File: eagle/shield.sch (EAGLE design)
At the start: 36 parts, among them Q1 REG1117, U1 TXB0104PWR, U2 TXB0104PWR

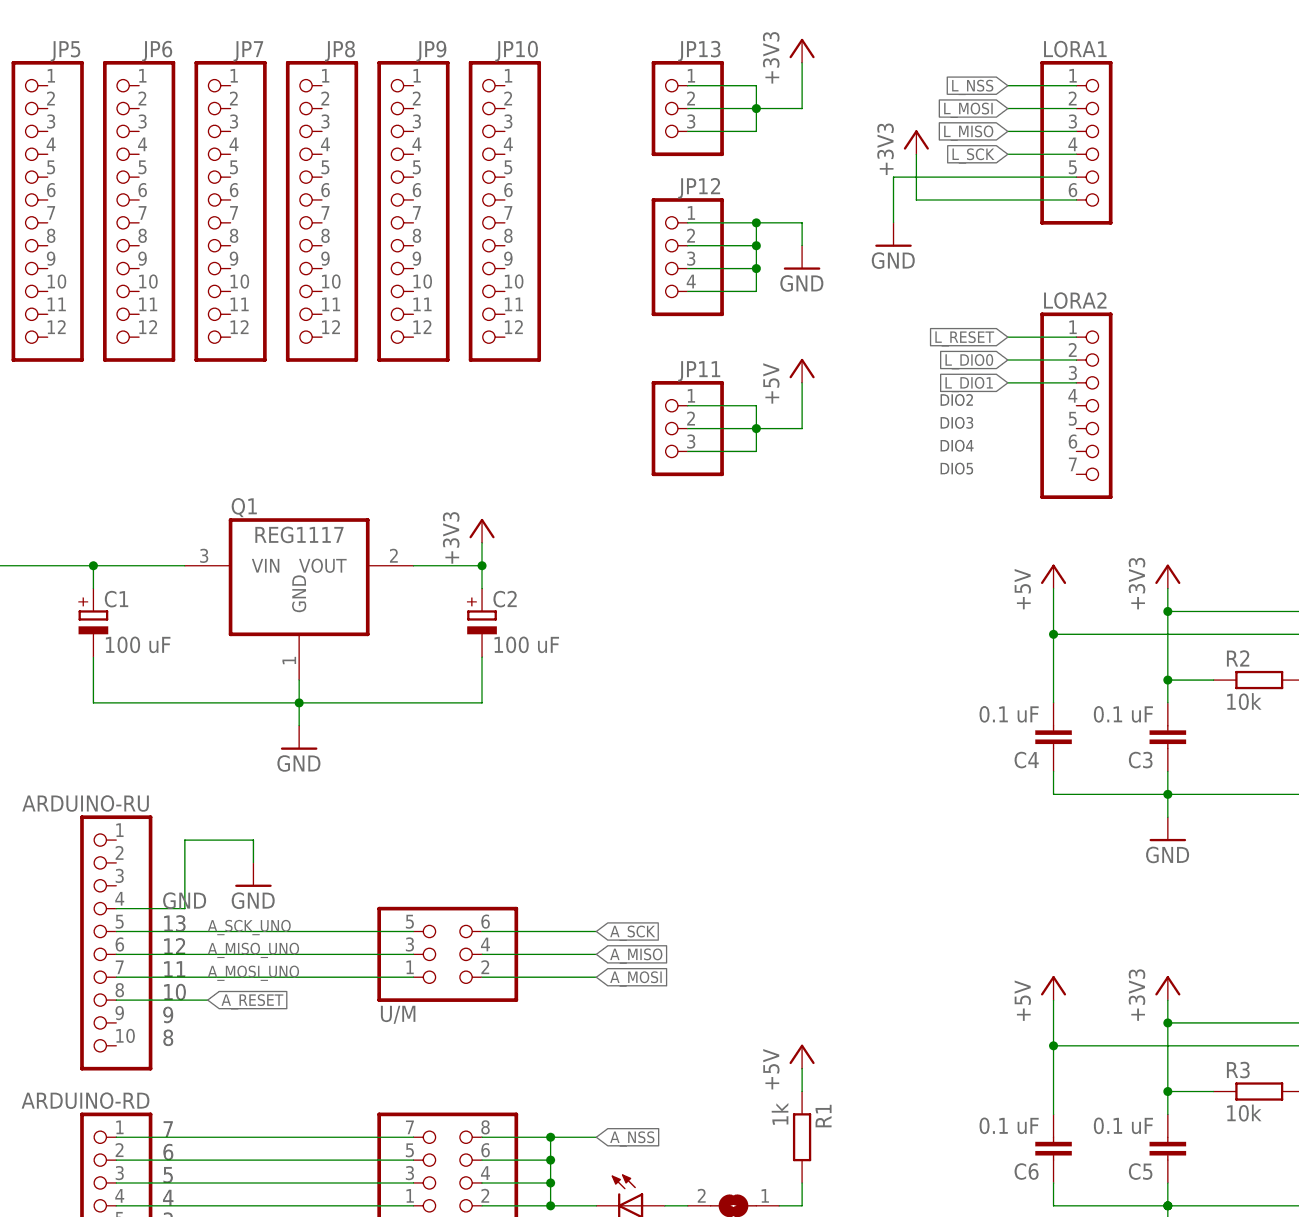
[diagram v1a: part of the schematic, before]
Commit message: Shield and breakout layout update
Added a gap to the pin headers on LoRa breakout board and the shield to enforce breakout orientation.
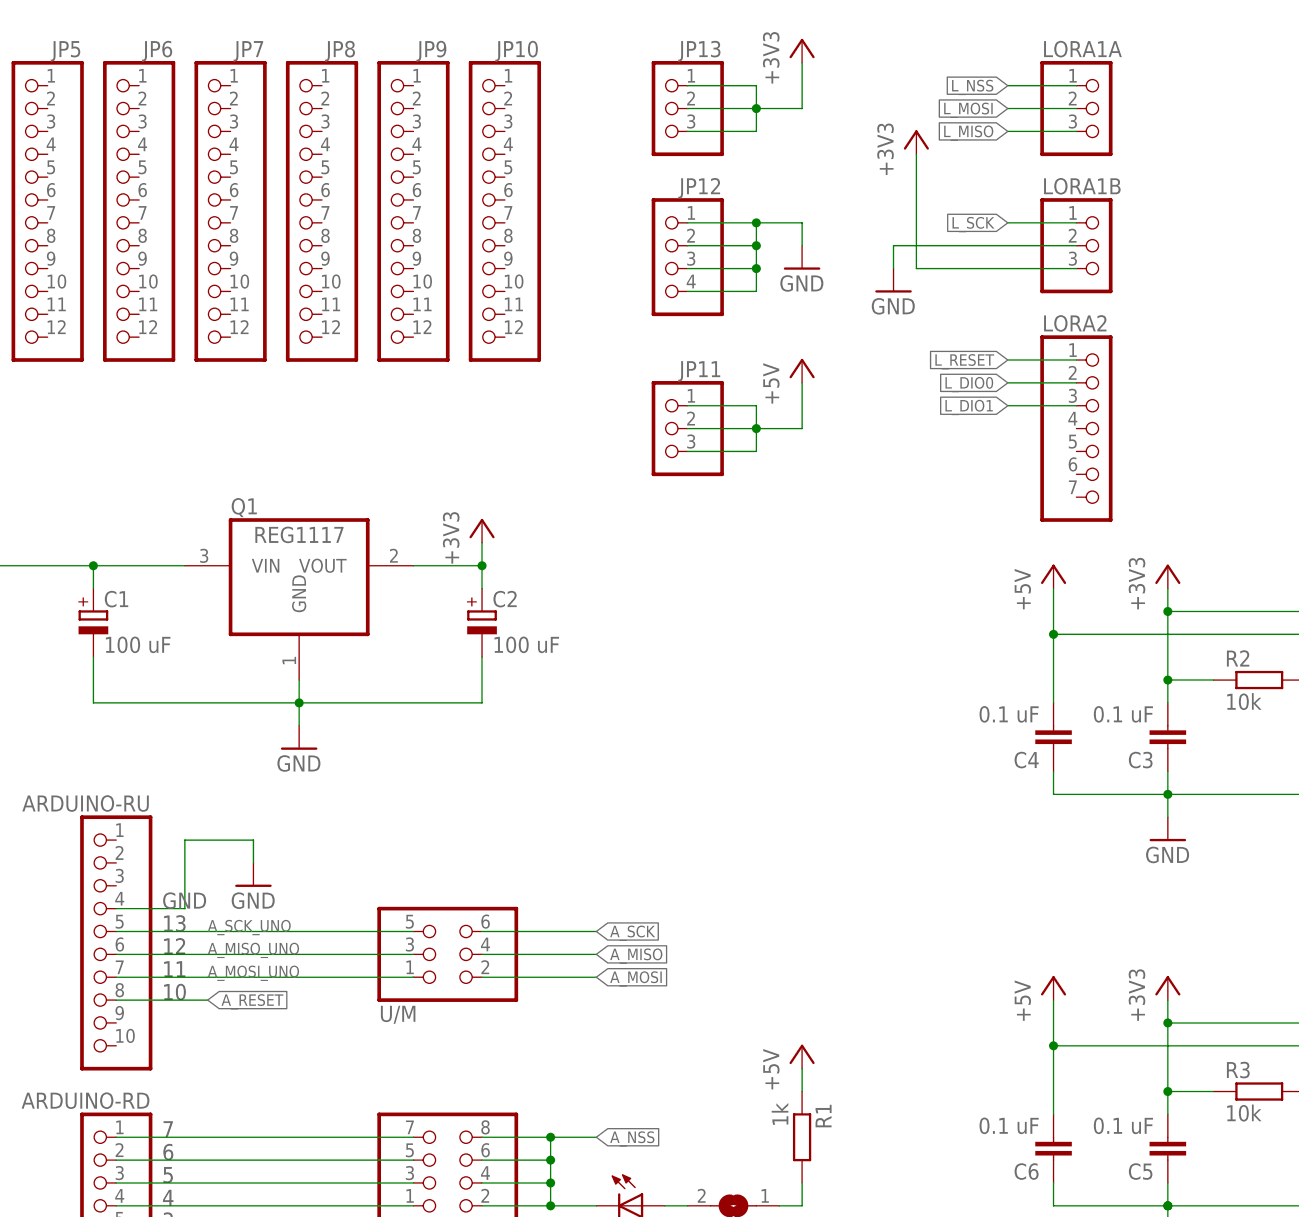
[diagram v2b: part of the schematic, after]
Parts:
- removed LORA1: (no value), pinhead:PINHD-1X6
- added LORA1A, LORA1B: (no value), pinhead:PINHD-1X3
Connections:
- net +3V3: now also LORA1B.3; no longer LORA1.6
- net GND: now also LORA1B.2; no longer LORA1.5
- net L_MISO: now also LORA1A.3; no longer LORA1.3
- net L_MOSI: now also LORA1A.2; no longer LORA1.2
- net L_NSS: now also LORA1A.1; no longer LORA1.1
- net L_SCK: now also LORA1B.1; no longer LORA1.4
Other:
- note removed: "8"
- note removed: "9"
- note removed: "DIO2"
- note removed: "DIO3"
- note removed: "DIO4"
- note removed: "DIO5"
- moved on the sheet: LORA2
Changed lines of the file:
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@@
 <setting verticaltext="up"/>
 </settings>
-<grid distance="0.5" unitdist="mil" unit="mil" style="lines" multiple="1" display="yes" altdistance="0.01" altunitdist="inch" altunit="inch"/>
+<grid distance="0.1" unitdist="inch" unit="inch" style="lines" multiple="1" display="no" altdistance="0.01" altunitdist="inch" altunit="inch"/>
 <layers>
 <layer number="1" name="Top" color="4" fill="1" visible="no" active="no"/>
@@
 <parts>
 <part name="POWER1" library="con-wago-500" deviceset="W237-102" device=""/>
-<part name="LORA1" library="pinhead" deviceset="PINHD-1X6" device=""/>
 <part name="LORA2" library="pinhead" deviceset="PINHD-1X7" device=""/>
 <part name="ARDUINO-LU" library="pinhead" deviceset="PINHD-1X8" device=""/>
@@
 <part name="R3" library="rcl" deviceset="R-EU_" device="R0603" value="10k"/>
 <part name="FRAME1" library="frames" deviceset="A4L-LOC" device=""/>
+<part name="LORA1A" library="pinhead" deviceset="PINHD-1X3" device=""/>
+<part name="LORA1B" library="pinhead" deviceset="PINHD-1X3" device=""/>
 </parts>
 <sheets>
@@
 <text x="68.58" y="66.04" size="1.778" layer="97">11</text>
 <text x="68.58" y="63.5" size="1.778" layer="97">10</text>
-<text x="154.94" y="129.54" size="1.27" layer="97">DIO2</text>
-<text x="154.94" y="127" size="1.27" layer="97">DIO3</text>
-<text x="154.94" y="124.46" size="1.27" layer="97">DIO4</text>
 <text x="68.58" y="48.26" size="1.778" layer="97">7</text>
 <text x="68.58" y="45.72" size="1.778" layer="97">6</text>
@@
 <text x="68.58" y="40.64" size="1.778" layer="97">4</text>
 <text x="68.58" y="38.1" size="1.778" layer="97">3</text>
-<text x="154.94" y="121.92" size="1.27" layer="97">DIO5</text>
-<text x="68.58" y="60.96" size="1.778" layer="97">9</text>
-<text x="68.58" y="58.42" size="1.778" layer="97">8</text>
 <text x="68.58" y="35.56" size="1.778" layer="97">2</text>
 <text x="149.86" y="20.32" size="1.778" layer="94" font="vector" ratio="16">LoRenz Rev.B Arduino shield</text>
@@
 <instance part="POWER1" gate="-1" x="17.78" y="121.92"/>
 <instance part="POWER1" gate="-2" x="17.78" y="111.76"/>
-<instance part="LORA1" gate="A" x="172.72" y="157.48"/>
-<instance part="LORA2" gate="A" x="172.72" y="129.54"/>
+<instance part="LORA2" gate="A" x="172.72" y="127"/>
 <instance part="ARDUINO-LU" gate="A" x="17.78" y="60.96" rot="MR0"/>
 <instance part="ARDUINO-RD" gate="A" x="60.96" y="38.1" rot="MR0"/>
@@
 <instance part="GND1" gate="1" x="40.64" y="55.88"/>
 <instance part="GND2" gate="1" x="33.02" y="116.84"/>
-<instance part="GND7" gate="1" x="149.86" y="147.32"/>
+<instance part="GND7" gate="1" x="149.86" y="142.24"/>
 <instance part="JP1" gate="G$1" x="12.7" y="152.4" rot="MR0"/>
 <instance part="JP2" gate="G$1" x="22.86" y="152.4" rot="MR0"/>
@@
 <instance part="R3" gate="G$1" x="190.5" y="53.34"/>
 <instance part="FRAME1" gate="G$1" x="0" y="0"/>
+<instance part="LORA1A" gate="A" x="172.72" y="162.56"/>
+<instance part="LORA1B" gate="A" x="172.72" y="147.32"/>
 </instances>
 <busses>
@@
 <net name="GND" class="0">
 <segment>
-<pinref part="LORA1" gate="A" pin="5"/>
 <pinref part="GND7" gate="1" pin="GND"/>
-<wire x1="170.18" y1="154.94" x2="149.86" y2="154.94" width="0.1524" layer="91"/>
-<wire x1="149.86" y1="154.94" x2="149.86" y2="149.86" width="0.1524" layer="91"/>
+<wire x1="170.18" y1="147.32" x2="149.86" y2="147.32" width="0.1524" layer="91"/>
+<wire x1="149.86" y1="147.32" x2="149.86" y2="144.78" width="0.1524" layer="91"/>
+<pinref part="LORA1B" gate="A" pin="2"/>
 </segment>
 <segment>
@@
 <net name="L_NSS" class="0">
 <segment>
-<pinref part="LORA1" gate="A" pin="1"/>
 <wire x1="170.18" y1="165.1" x2="162.56" y2="165.1" width="0.1524" layer="91"/>
 <label x="162.56" y="165.1" size="1.27" layer="95" rot="R180" xref="yes"/>
+<pinref part="LORA1A" gate="A" pin="1"/>
 </segment>
 <segment>
@@
 <net name="L_MOSI" class="0">
 <segment>
-<pinref part="LORA1" gate="A" pin="2"/>
 <wire x1="170.18" y1="162.56" x2="162.56" y2="162.56" width="0.1524" layer="91"/>
 <label x="162.56" y="162.56" size="1.27" layer="95" rot="R180" xref="yes"/>
+<pinref part="LORA1A" gate="A" pin="2"/>
 </segment>
 <segment>
@@
 <net name="L_MISO" class="0">
 <segment>
-<pinref part="LORA1" gate="A" pin="3"/>
 <wire x1="170.18" y1="160.02" x2="162.56" y2="160.02" width="0.1524" layer="91"/>
 <label x="162.56" y="160.02" size="1.27" layer="95" rot="R180" xref="yes"/>
+<pinref part="LORA1A" gate="A" pin="3"/>
 </segment>
 <segment>
@@
 <net name="L_SCK" class="0">
 <segment>
-<pinref part="LORA1" gate="A" pin="4"/>
-<wire x1="170.18" y1="157.48" x2="162.56" y2="157.48" width="0.1524" layer="91"/>
-<label x="162.56" y="157.48" size="1.27" layer="95" rot="R180" xref="yes"/>
+<wire x1="170.18" y1="149.86" x2="162.56" y2="149.86" width="0.1524" layer="91"/>
+<label x="162.56" y="149.86" size="1.27" layer="95" rot="R180" xref="yes"/>
+<pinref part="LORA1B" gate="A" pin="1"/>
 </segment>
 <segment>
@@
 <segment>
 <pinref part="LORA2" gate="A" pin="1"/>
-<wire x1="170.18" y1="137.16" x2="162.56" y2="137.16" width="0.1524" layer="91"/>
-<label x="162.56" y="137.16" size="1.27" layer="95" rot="R180" xref="yes"/>
+<wire x1="170.18" y1="134.62" x2="162.56" y2="134.62" width="0.1524" layer="91"/>
+<label x="162.56" y="134.62" size="1.27" layer="95" rot="R180" xref="yes"/>
 </segment>
 <segment>
@@
 <segment>
 <pinref part="LORA2" gate="A" pin="2"/>
-<wire x1="170.18" y1="134.62" x2="162.56" y2="134.62" width="0.1524" layer="91"/>
-<label x="162.56" y="134.62" size="1.27" layer="95" rot="R180" xref="yes"/>
+<wire x1="170.18" y1="132.08" x2="162.56" y2="132.08" width="0.1524" layer="91"/>
+<label x="162.56" y="132.08" size="1.27" layer="95" rot="R180" xref="yes"/>
 </segment>
 <segment>
@@
 <segment>
 <pinref part="LORA2" gate="A" pin="3"/>
-<wire x1="170.18" y1="132.08" x2="162.56" y2="132.08" width="0.1524" layer="91"/>
-<label x="162.56" y="132.08" size="1.27" layer="95" rot="R180" xref="yes"/>
+<wire x1="170.18" y1="129.54" x2="162.56" y2="129.54" width="0.1524" layer="91"/>
+<label x="162.56" y="129.54" size="1.27" layer="95" rot="R180" xref="yes"/>
 </segment>
 <segment>
@@
 </segment>
 <segment>
-<pinref part="LORA1" gate="A" pin="6"/>
-<wire x1="170.18" y1="152.4" x2="152.4" y2="152.4" width="0.1524" layer="91"/>
-<wire x1="152.4" y1="152.4" x2="152.4" y2="157.48" width="0.1524" layer="91"/>
+<wire x1="170.18" y1="144.78" x2="152.4" y2="144.78" width="0.1524" layer="91"/>
+<wire x1="152.4" y1="144.78" x2="152.4" y2="157.48" width="0.1524" layer="91"/>
 <pinref part="+3V3" gate="G$1" pin="+3V3"/>
-</segment>
-<segment>
+<pinref part="LORA1B" gate="A" pin="3"/>
+</segment>
+<segment>

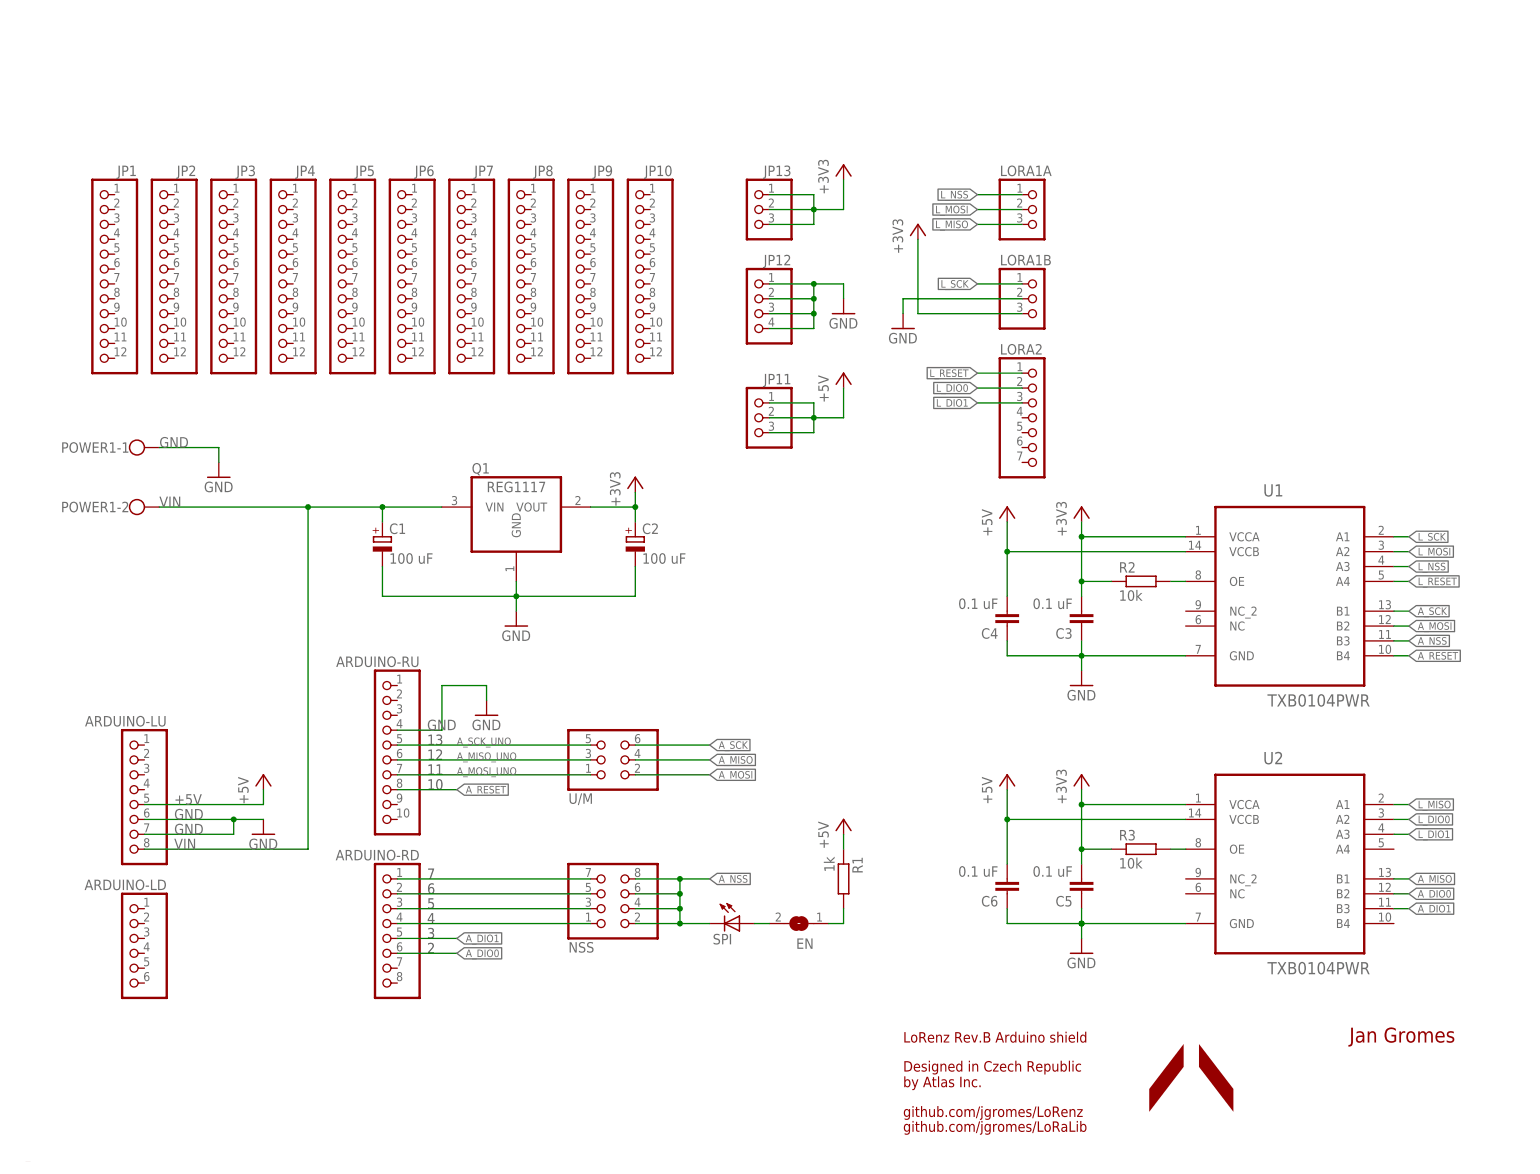
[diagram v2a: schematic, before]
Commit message: Changed package of C2
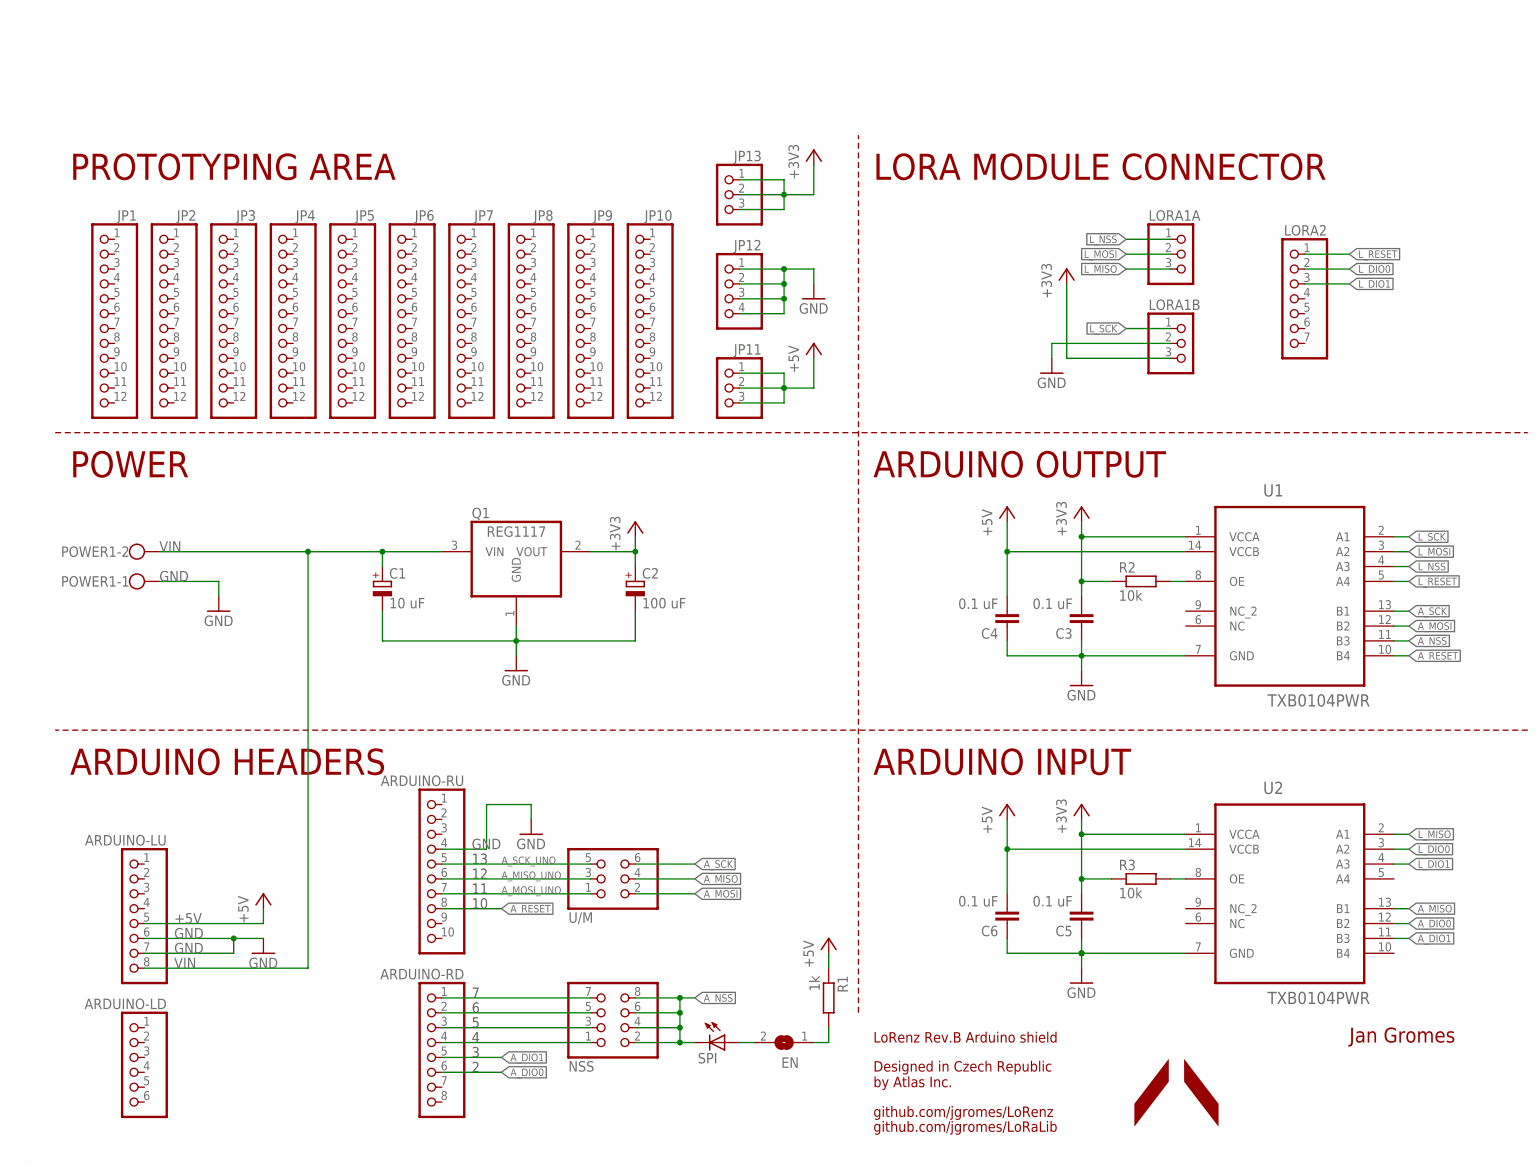
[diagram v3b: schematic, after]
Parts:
- C1: value 100 uF -> 10 uF; device rcl:CPOL-EUSMCD -> rcl:CPOL-EUSMCA
- C2: device rcl:CPOL-EUSMCD -> rcl:CPOL-EUSMCB
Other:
- note added: "ARDUINO HEADERS"
- note added: "ARDUINO INPUT"
- note added: "ARDUINO OUTPUT"
- note added: "LORA MODULE CONNECTOR"
- note added: "POWER"
- note added: "PROTOTYPING AREA"
- moved on the sheet: ARDUINO-LD, ARDUINO-LU, ARDUINO-RD, ARDUINO-RU, C1, C2, C5, C6, EN, JP1, JP10, JP11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
